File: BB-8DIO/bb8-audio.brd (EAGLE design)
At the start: 79.7 x 47 mm, 28 parts, among them IC1 7805L, IC3 74LS125N

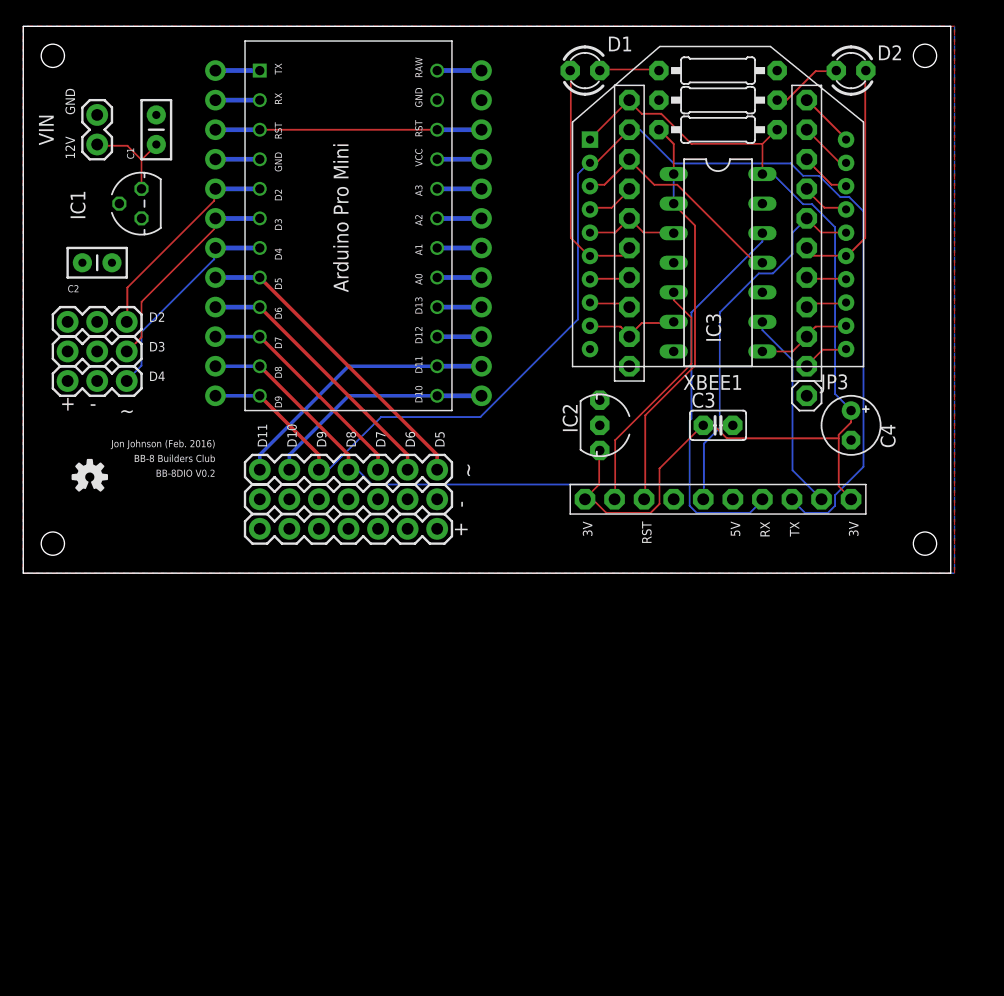
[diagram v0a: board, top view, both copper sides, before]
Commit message: Revision 0.3 of the BB-8DIO board.
Adding revision 0.3. This has the audio breakout board footprint so the
breakout can be dropped on using header pins. This also has reworked a
lot of other pins and headers have been removed because they are no
longer available after adding the audio breakout. Resolved some
silkscreen issues and also resolved issues with 5V on arduino input and
Xbee input.
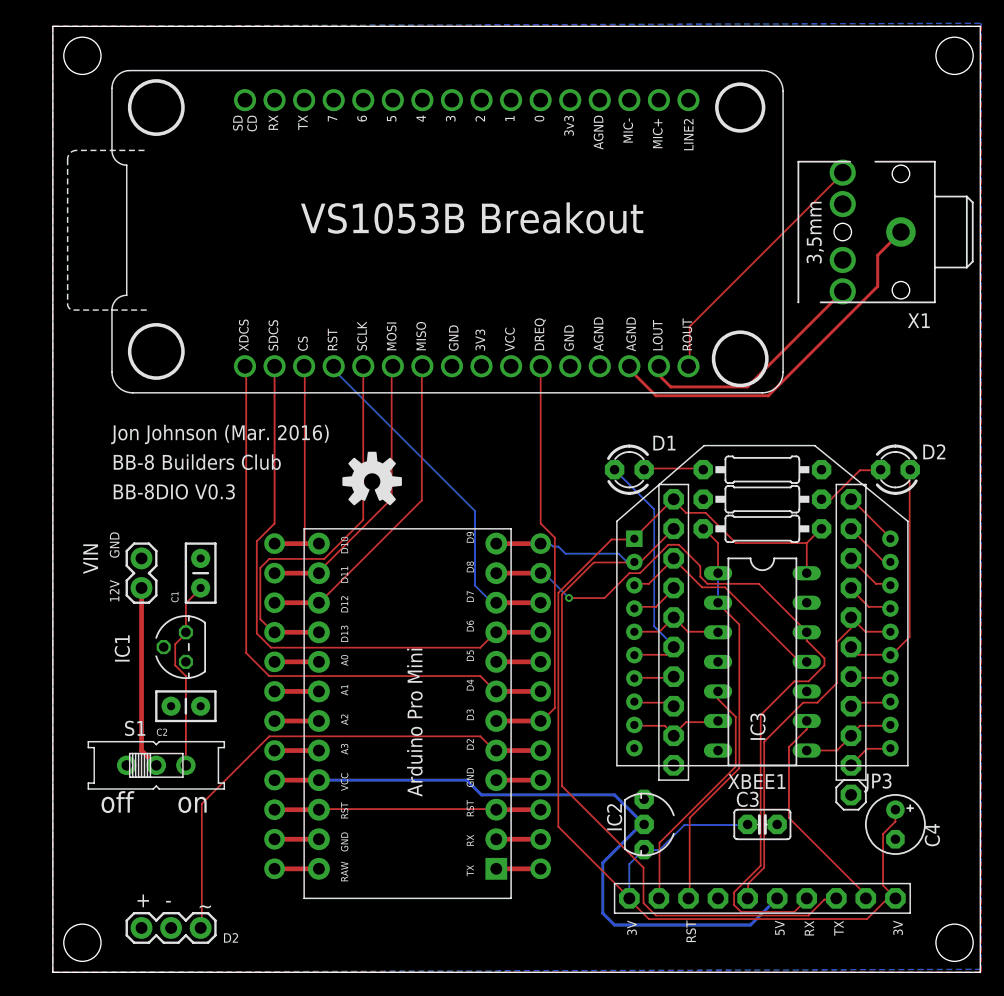
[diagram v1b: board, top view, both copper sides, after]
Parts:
- removed +, -, ~: (no value), SparkFun-Connectors:1X07
- removed LEDS2: LEDS2, SparkFun-Connectors:1X03
- removed LEDS3: LEDS3, SparkFun-Connectors:1X03
- removed U$1: (no value), Spark:OSHW-LOGO-S
- added S1: (no value), adafruit:EG1218
- added U$3: (no value), Spark:OSHW-LOGO-M
- added VS1053B: VS1053B_BREAKOUT, VS1053B_BREAKOUT:VS1053_BREAKOUT
- added X1: STEREOJACK, adafruit:STX3100
- moved LEDS1 52.5 mm to (12.7, 3.81)
- moved JP1 49.3 mm to (41.9, 22.9), turned to 270 degrees
- moved JP2 44.4 mm to (19.1, 22.9), turned to 90 degrees
- moved ARD_PRO_MINI 43.5 mm to (30.5, 21.6), turned to 180 degrees
- moved C2 38.9 mm to (10.2, 22.9)
- moved IC1 38.3 mm to (11.4, 27.9)
- moved C1 38.3 mm to (12.7, 33.0)
- moved VIN 38.3 mm to (7.62, 33.0)
- moved C3 34.5 mm to (61.0, 12.7)
- moved C4 34.5 mm to (72.4, 12.7)
- moved IC2 34.5 mm to (50.8, 12.7)
- moved R2 34.5 mm to (61.0, 40.6)
- moved XBEE1 34.5 mm to (61.0, 31.8)
- moved D1 34.5 mm to (49.5, 43.2)
- moved D2 34.5 mm to (72.4, 43.2)
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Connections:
- removed net VCC: ARD_PRO_MINI.VCC, JP2.4
- new net AGND1: VS1053B.AGND1, X1.1
- new net N$25: VS1053B.ROUT, X1.5
- new net N$26: S1.P, VIN.1
- net 5V: now also ARD_PRO_MINI.VCC, JP2.4, LEDS1.3, VS1053B.VCC; no longer +.1, +.2, +.3, +.4, +.5, +.6, +.7, LEDS1.2, LEDS2.2, LEDS3.2
- net D10: now also VS1053B.CS; no longer ~.6
- net D11: now also VS1053B.MOSI; no longer ~.7
- net D12: now also VS1053B.MISO
- net D13: now also VS1053B.SCLK
- net D3: now also VS1053B.DREQ; no longer LEDS2.1
- net D4: now also VS1053B.XDCS; no longer LEDS3.1
- net D5: no longer ~.1
- net D6: now also VS1053B.SDCS; no longer ~.2
- net D7: now also VS1053B.RST; no longer ~.3
- net D8: no longer ~.4
- net D9: no longer ~.5
- net GND: now also LEDS1.2, U$6.7, VS1053B.GND, VS1053B.GND1; no longer -.1, -.2, -.3, -.4, -.5, -.6, -.7, LEDS1.3, LEDS2.3, LEDS3.3
- net N$2: now also S1.S; no longer VIN.1
- net N$21: now also VS1053B.LOUT, X1.2; no longer U$6.7
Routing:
- net 5V: track 0.00 -> 58.9 mm
- net D9: track 112.2 -> 71.6 mm
- net D4: track 18.4 -> 51.3 mm
- net AGND1: track 0.00 -> 31.9 mm
- net D13: track 3.81 -> 33.7 mm
- net D6: track 23.0 -> 49.0 mm
- net D2: track 18.4 -> 42.8 mm
- net D12: track 3.81 -> 27.8 mm
- net D5: track 26.6 -> 3.81 mm
- net N$25: track 0.00 -> 22.1 mm
- net N$21: track 0.00 -> 20.4 mm
- net 3.3V: track 87.9 -> 107.2 mm
- net D3: track 18.5 -> 35.3 mm
- net N$26: track 0.00 -> 15.8 mm
- net D7: track 19.4 -> 30.2 mm
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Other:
- board size 79.7 x 47 mm -> 79.7 x 81.3 mm
- board text added: "BB-8DIO V0.3"
- board text added: "Jon Johnson (Mar. 2016)"
- board text added: "off"
- board text added: "on"
- board text removed: "BB-8DIO V0.2"
- board text removed: "D10"
- board text removed: "D11"
- board text removed: "D3"
- board text removed: "D4"
- board text removed: "D5"
- board text removed: "D6"
- board text removed: "D7"
- board text removed: "D8"
- board text removed: "D9"
- board text removed: "Jon Johnson (Feb. 2016)"
